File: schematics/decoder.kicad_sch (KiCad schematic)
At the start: 1 part, among them U12 ATF22V10C-7

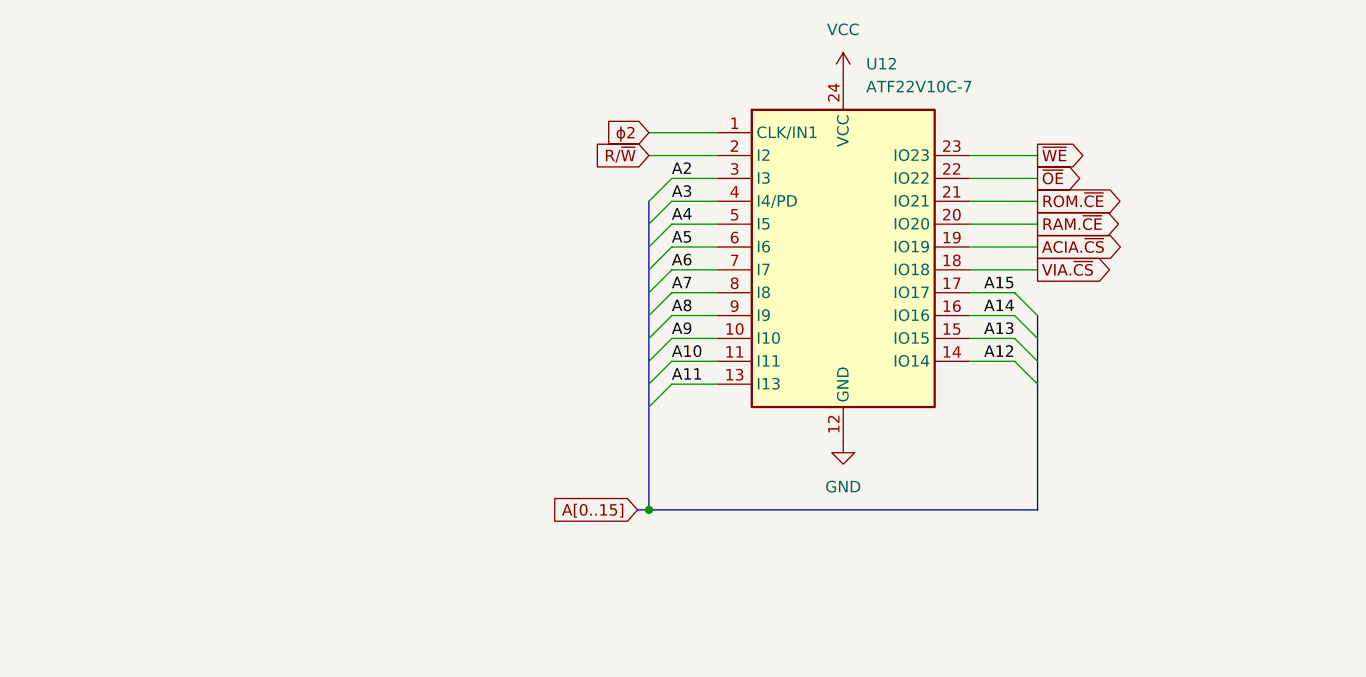
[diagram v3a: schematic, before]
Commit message: PLD files and schematics for address decoder, device selector, keyboard controller, lcd controller, banked memory, and bootloader.
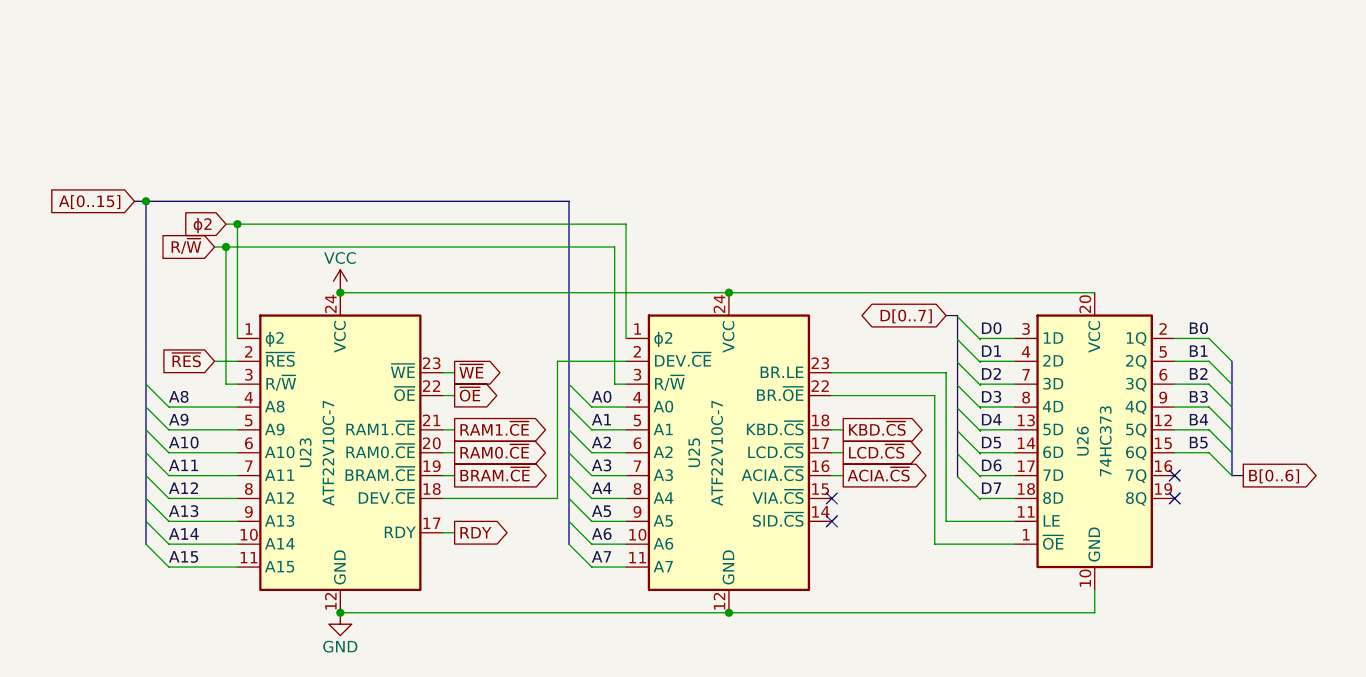
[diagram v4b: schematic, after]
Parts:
- removed U12: ATF22V10C-7, Package_DIP:DIP-24_W7.62mm, symbol Logic_Programmable:PEEL22CV10AP
- added U23, U25: ATF22V10C-7, Package_DIP:DIP-24_W7.62mm, symbol Logic_Programmable:PEEL22CV10AP
- added U26: 74HC373, symbol 74xx:74HC373
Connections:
- net A10: now also U23.6 (A10)
- net A11: now also U23.7 (A11)
- net A12: now also U23.8 (A12)
- net A13: now also U23.9 (A13)
- net A14: now also U23.10 (A14)
- net A15: now also U23.11 (A15)
- net A2: now also U25.6 (A2)
- net A3: now also U25.7 (A3)
- net A4: now also U25.8 (A4)
- net A5: now also U25.9 (A5)
- net A6: now also U25.10 (A6)
- net A7: now also U25.11 (A7)
- net A8: now also U23.4 (A8)
- net A9: now also U23.5 (A9)
- net ACIA.~{CS}: now also U25.16 (ACIA.~{CS})
- net GND: now also U23.12 (GND), U25.12 (GND), U26.10 (GND)
- net R/~{W}: now also U23.3 (R/~{W}), U25.3 (R/~{W})
- net VCC: now also U23.24 (VCC), U25.24 (VCC), U26.20 (VCC)
- net ~{OE}: now also U23.22 (~{OE})
- net ~{WE}: now also U23.23 (~{WE})
- net ϕ2: now also U23.1 (ϕ2), U25.1 (ϕ2)
- new net: U25.22 (BR.~{OE}), U26.1 (~{OE})
- new net: U25.23 (BR.LE), U26.11 (LE)
- new net: U23.18 (DEV.~{CE}), U25.2 (DEV.~{CE})
- new net A0: U25.4 (A0)
- new net A1: U25.5 (A1)
- new net B0: U26.2 (1Q)
- new net B1: U26.5 (2Q)
- new net B2: U26.6 (3Q)
- new net B3: U26.9 (4Q)
- new net B4: U26.12 (5Q)
- new net B5: U26.15 (6Q)
- new net BRAM.~{CE}: U23.19 (BRAM.~{CE})
- new net D0: U26.3 (1D)
- new net D1: U26.4 (2D)
- new net D2: U26.7 (3D)
- new net D3: U26.8 (4D)
- new net D4: U26.13 (5D)
- new net D5: U26.14 (6D)
- new net D6: U26.17 (7D)
- new net D7: U26.18 (8D)
- new net KBD.~{CS}: U25.18 (KBD.~{CS})
- new net LCD.~{CS}: U25.17 (LCD.~{CS})
- new net RAM0.~{CE}: U23.20 (RAM0.~{CE})
- new net RAM1.~{CE}: U23.21 (RAM1.~{CE})
- new net RDY: U23.17 (RDY)
- new net ~{RES}: U23.2 (~{RES})
- no-connect marks 0 -> 4

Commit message: added phi0 for write latch timing
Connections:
- net A0: now also U25.5 (A0); no longer U25.4 (A0)
- net A1: now also U25.6 (A1); no longer U25.5 (A1)
- net A10: now also U23.7 (A10); no longer U23.6 (A10)
- net A11: now also U23.8 (A11); no longer U23.7 (A11)
- net A12: now also U23.9 (A12); no longer U23.8 (A12)
- net A13: now also U23.10 (A13); no longer U23.9 (A13)
- net A14: now also U23.11 (A14); no longer U23.10 (A14)
- net A15: now also U23.13 (A15); no longer U23.11 (A15)
- net A2: now also U25.7 (A2); no longer U25.6 (A2)
- net A3: now also U25.8 (A3); no longer U25.7 (A3)
- net A4: now also U25.9 (A4); no longer U25.8 (A4)
- net A5: now also U25.10 (A5); no longer U25.9 (A5)
- net A6: now also U25.11 (A6); no longer U25.10 (A6)
- net A7: now also U25.13 (A7); no longer U25.11 (A7)
- net A8: now also U23.5 (A8); no longer U23.4 (A8)
- net A9: now also U23.6 (A9); no longer U23.5 (A9)
- net R/~{W}: now also U23.4 (R/~{W}), U25.4 (R/~{W}); no longer U23.3 (R/~{W}), U25.3 (R/~{W})
- net ~{RES}: now also U23.3 (~{RES}); no longer U23.2 (~{RES})
- net VIA.~{CS}: now reaches U25.15 (VIA.~{CS})
- net at U23.18 (DEV.~{CE}): now also U25.3 (DEV.~{CE}); no longer U25.2 (DEV.~{CE})
- new net ϕ0: U23.2 (ϕ0), U25.2 (ϕ0)
- no-connect marks 4 -> 3
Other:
- moved on the sheet: U26

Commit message: updating schematics as I wire the board
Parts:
- renumbered U25 to U10, U26 to U11, U23 to U9
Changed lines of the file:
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@@
 		(in_pos_files yes)
 		(dnp no)
-		(property "Reference" "#PWR026"
+		(property "Reference" "#PWR023"
 			(at 143.51 93.98 0)
 			(hide yes)
@@
 			(project "bv6502_hw"
 				(path "/94c72abe-aaa5-49aa-8ab7-5d3e7cbc10be/84bb5624-3de3-475d-b983-481178beada9"
-					(reference "#PWR026")
+					(reference "#PWR023")
 					(unit 1)
 				)
@@
 		(dnp no)
 		(fields_autoplaced yes)
-		(property "Reference" "U26"
+		(property "Reference" "U11"
 			(at 182.88 106.68 90)
 			(show_name no)
@@
 			(project "bv6502_hw"
 				(path "/94c72abe-aaa5-49aa-8ab7-5d3e7cbc10be/84bb5624-3de3-475d-b983-481178beada9"
-					(reference "U26")
+					(reference "U11")
 					(unit 1)
 				)
@@
 		(in_pos_files yes)
 		(dnp no)
-		(property "Reference" "#PWR030"
+		(property "Reference" "#PWR024"
 			(at 143.51 134.62 0)
 			(hide yes)
@@
 			(project "bv6502_hw"
 				(path "/94c72abe-aaa5-49aa-8ab7-5d3e7cbc10be/84bb5624-3de3-475d-b983-481178beada9"
-					(reference "#PWR030")
+					(reference "#PWR024")
 					(unit 1)
 				)
@@
 		(in_pos_files yes)
 		(dnp no)
-		(property "Reference" "U25"
+		(property "Reference" "U10"
 			(at 139.7 107.95 90)
 			(show_name no)
@@
 			(project "bv6502_hw"
 				(path "/94c72abe-aaa5-49aa-8ab7-5d3e7cbc10be/84bb5624-3de3-475d-b983-481178beada9"
-					(reference "U25")
+					(reference "U10")
 					(unit 1)
 				)
@@
 		(in_pos_files yes)
 		(dnp no)
-		(property "Reference" "U23"
+		(property "Reference" "U9"
 			(at 96.52 109.22 90)
 			(show_name no)
@@
 			(project "bv6502_hw"
 				(path "/94c72abe-aaa5-49aa-8ab7-5d3e7cbc10be/84bb5624-3de3-475d-b983-481178beada9"
-					(reference "U23")
+					(reference "U9")
 					(unit 1)
 				)

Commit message: updating schematics as I wire the board
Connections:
- net ϕ0: now also U10.1 (ϕ0), U9.1 (ϕ0); no longer U10.2 (ϕ0), U9.2 (ϕ0)
- net ϕ2: now also U10.2 (ϕ2), U9.2 (ϕ2); no longer U10.1 (ϕ2), U9.1 (ϕ2)
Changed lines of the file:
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@@
 		)
 	)
-	(global_label "ϕ0"
+	(global_label "ϕ2"
 		(shape input)
 		(at 83.82 86.36 180)
@@
 		)
 	)
-	(global_label "ϕ2"
+	(global_label "ϕ0"
 		(shape input)
 		(at 83.82 83.82 180)
@@
 		)
 	)
-	(global_label "B[0..6]"
+	(global_label "B[0..5]"
 		(shape output)
 		(at 200.66 110.49 0)

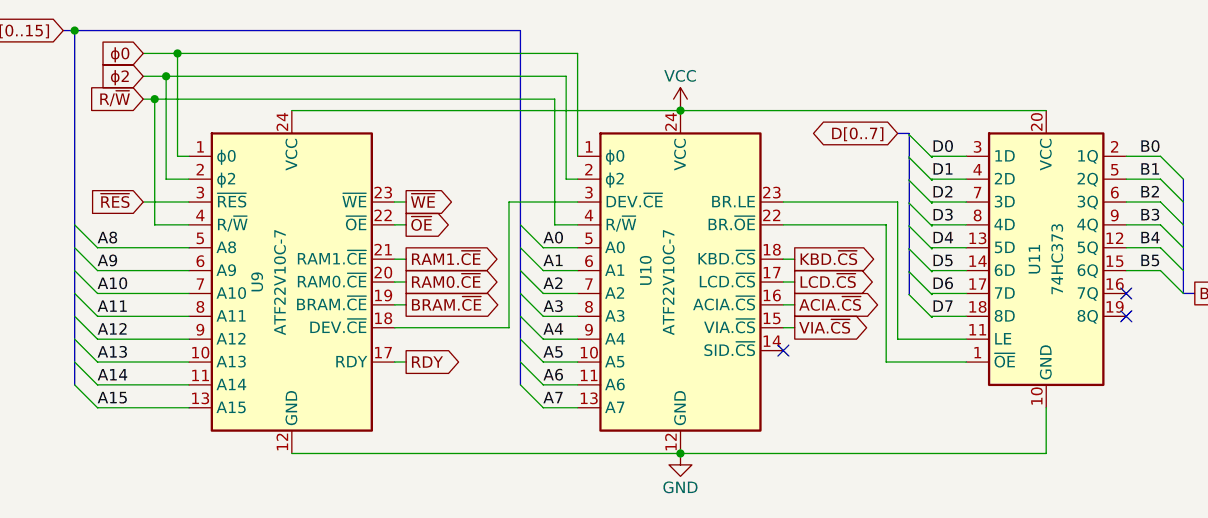
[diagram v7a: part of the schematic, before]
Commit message: forgot bank register transciever so now it's write-only
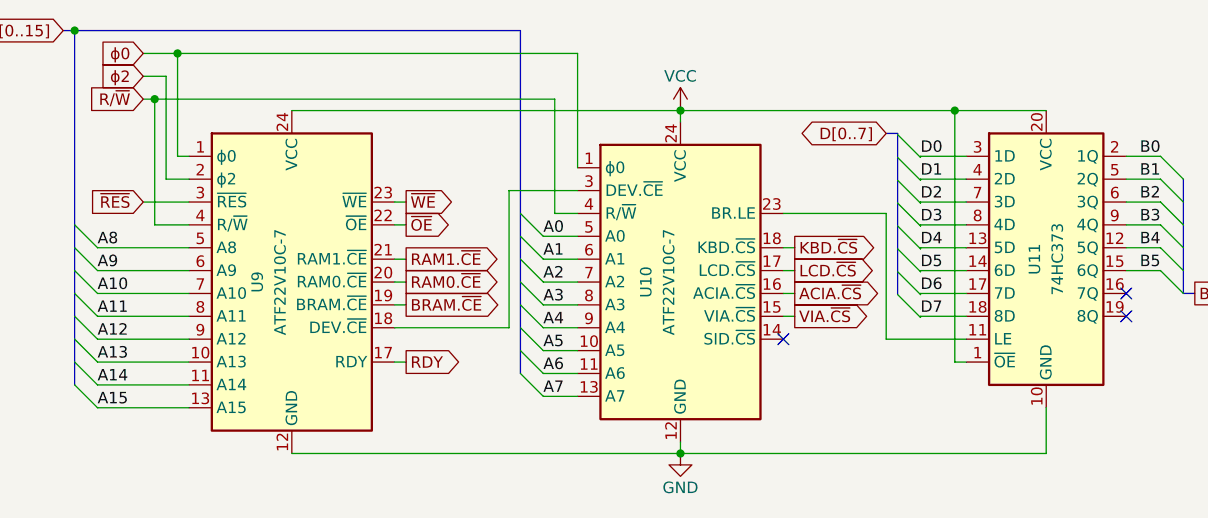
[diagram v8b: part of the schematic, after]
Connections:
- net VCC: now also U11.1 (~{OE})
- net ϕ2: no longer U10.2 (ϕ2)
- net at U10.22 (BR.~{OE}): no longer U11.1 (~{OE})
